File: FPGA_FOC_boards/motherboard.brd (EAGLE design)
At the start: 76.2 x 80 mm, 148 parts, among them J1 PRIUS_INV_DB26, U1 ADS7883, U10 ADS7883, U11 ADS7883, U12 ADS7883, U13 LM7321, U14 LM7321, U15 LM7321, U16 LM7321, U17 CD40109BPWR, U18 CD40109BPWR, U19 LM7321, U2 ADS7883, U20 CMOD_A7, U3 ADS7883, U4 ADS7883, U5 LM7321, U6 LM7321, U7 LM7321, U8 LM7321, U9 ADS7883

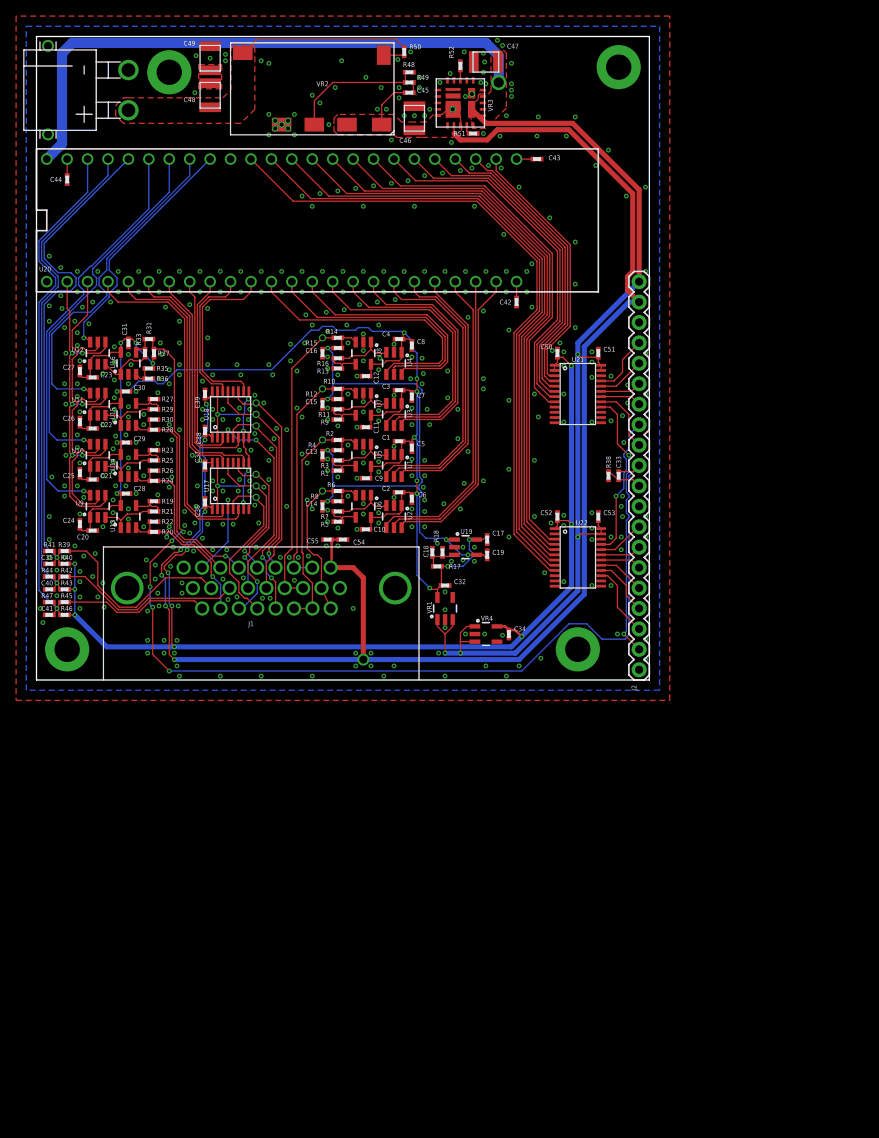
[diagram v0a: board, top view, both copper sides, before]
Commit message: started adding in the resolver hardware onto the motherboard, began ripping up some parts of the v1 board to make room for resolver hardware
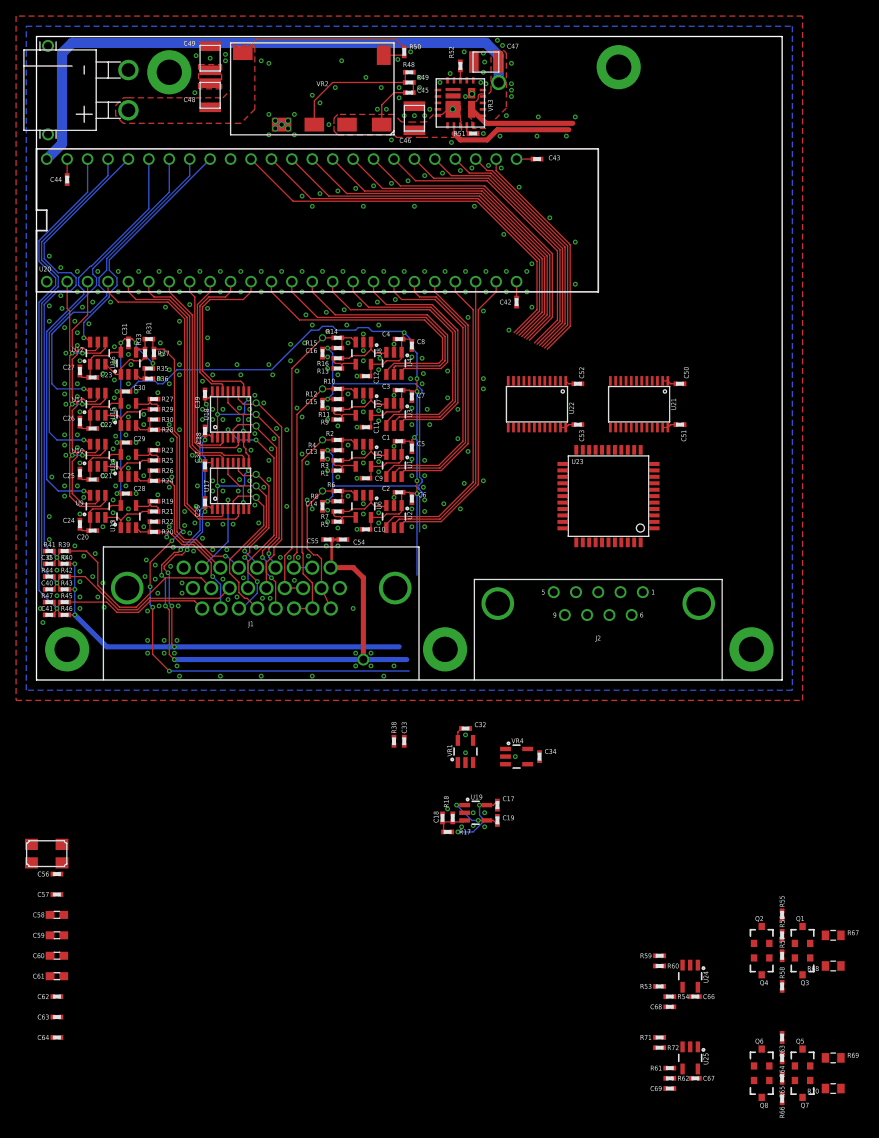
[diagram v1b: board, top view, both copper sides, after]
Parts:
- added C56, C57: 20p, FPGA_FOC_lib:0402
- added C58, C59, C60, C61: 10u, FPGA_FOC_lib:0603
- added C62, C63, C64: 10n, FPGA_FOC_lib:0402
- added C66, C67, C68, C69, R53, R54, R55, R56, R57, R58, R61, R62, R63, R64, R65, R66: (no value), FPGA_FOC_lib:0402
- added H5: BOLTHOLE_M3, FPGA_FOC_lib:M3_HOLE
- added Q1, Q2, Q3, Q4, Q5, Q6, Q7, Q8: (no value), FPGA_FOC_lib:SOT23-3
- added R59, R60, R71, R72: 1k, FPGA_FOC_lib:0402
- added R67, R68, R69, R70: 16, FPGA_FOC_lib:0805
- added U23: ADS1205, FPGA_FOC_lib:LQFP44
- added U24, U25: LM7321, FPGA_FOC_lib:SOT23-5
- added Y1: 8.192mHz, FPGA_FOC_lib:5X3.2MM_SMD_XTAL
- J2: value (none) -> DB09_RA; device FPGA_FOC_lib:1X20 -> FPGA_FOC_lib:AE10921
- R36: value (none) -> 10k
- moved C33 42.4 mm to (45.7, -7.62)
- moved R38 42.4 mm to (44.5, -7.62)
- moved U19 33.0 mm to (54.6, -16.5)
- moved C17 33.0 mm to (57.3, -15.6)
- moved C18 33.0 mm to (50.5, -17.1)
- moved C19 33.0 mm to (57.3, -17.5)
- moved R17 33.0 mm to (51.1, -18.9)
- moved R18 33.0 mm to (51.8, -17.1)
- moved U22 19.7 mm to (62.2, 34.3), turned to 270 degrees
- moved C32 18.0 mm to (53.3, -6.03)
- moved VR1 18.0 mm to (53.3, -8.89)
- moved C52 16.7 mm to (67.3, 36.8), turned to 0 degrees
- moved H1 16.5 mm to (50.8, 3.81)
- moved C50 15.7 mm to (80.0, 36.8), turned to 0 degrees
- moved C34 15.7 mm to (62.5, -9.53)
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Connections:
- new net !RD_EXC: R61.1, U23.35
- new net !RD_EXCOUT: C69.2, J2.9, R62.1, R69.2, R70.1
- new net MT1: J2.6
- new net MT2: J2.7
- new net M_CASE: J2.8
- new net Q1_BASE: Q1.1, R55.2, R56.1
- new net Q1_EMITTER: Q1.2, R67.1
- new net Q2_BC: Q2.1, Q2.3, R56.2
- new net Q3_BASE: Q3.1, R57.2, R58.1
- new net Q3_EMITTER: Q3.2, R68.2
- new net Q4_BC: Q4.1, Q4.3, R57.1
- new net Q5_BASE: Q5.1, R63.1, R64.2
- new net Q5_EMITTER: Q5.2, R69.1
- new net Q6_BC: Q6.1, Q6.3, R64.1
- new net Q7_BASE: Q7.1, R65.1, R66.2
- new net Q7_EMITTER: Q7.2, R70.2
- new net Q8_BC: Q8.1, Q8.3, R65.2
- new net RD_CLKIN: C57.1, U23.22, Y1.3
- new net RD_COS: J2.1, U23.41
- new net RD_COSLO: J2.2, U23.40
- new net RD_CPO: U23.24
- new net RD_EXC: R53.1, U23.34
- new net RD_EXCOUT: C68.2, J2.5, R54.1, R67.2, R68.1
- new net RD_REFBYP: C58.1, U23.43
- new net RD_SIN: J2.4, U23.37
- new net RD_SINLO: J2.3, U23.38
- new net RD_XTALOUT: C56.2, U23.21, Y1.1
- new net U24_IN+: R59.2, R60.1, U24.3
- new net U24_IN-: C68.1, R53.2, R54.2, U24.4
- new net U24_OUT: Q2.2, Q4.2, U24.1
- new net U25_IN+: R71.2, R72.1, U25.3
- new net U25_IN-: C69.1, R61.2, R62.2, U25.4
- new net U25_OUT: Q6.2, Q8.2, U25.1
- net !RD_CS: now also U23.3; no longer J2.16
- net !RD_DOS: now also U23.29; no longer J2.4
- net !RD_LOT: now also U23.30; no longer J2.3
- net !RD_RD: now also U23.2; no longer J2.17
- net !RD_RDVEL: now also U23.5; no longer J2.14
- net !RD_RESET: now also U23.33; no longer J2.2
- net !RD_SAMPLE: now also U23.4; no longer J2.15
- net 12V: now also C66.1, C67.1, Q1.3, Q5.3, R55.1, R63.2, U24.5, U25.5; no longer J2.19
- net 5V: now also C59.1, C60.1, C61.1, C62.1, C63.1, C64.1, R59.1, R71.1, U23.1, U23.17, U23.31, U23.32, U23.39; no longer J2.20
- net GND: now also C56.1, C57.2, C58.2, C59.2, C60.2, C61.2, C62.2, C63.2, C64.2, C66.2, C67.2, H5.P, J2.ML, J2.MR, Q3.3, Q7.3, R58.2, R60.2, R66.1, R72.2, U23.16, U23.23, U23.36, U23.42, U23.6, U24.2, U25.2, Y1.2, Y1.4; no longer J2.1, J2.18, J2.9
- net RD_A: now also U23.25; no longer J2.8
- net RD_B: now also U23.26; no longer J2.7
- net RD_DIR: now also U23.28; no longer J2.5
- net RD_MT1: no longer J2.11
- net RD_MT2: no longer J2.10
- net RD_NM: now also U23.27; no longer J2.6
- net RD_SCLK: now also U23.8; no longer J2.12
- net RD_SO: now also U23.7; no longer J2.13
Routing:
- net 5V: track 193.1 -> 89.7 mm, vias 5 -> 1
- net 12V: track 200.5 -> 109.6 mm
- net 3.3V: track 145.7 -> 86.0 mm, vias 12 -> 9
- net RD_MT1: track 132.3 -> 76.3 mm
- net !RD_RESET: track 33.8 -> 0.00 mm, vias 2 -> 0
- net !RD_LOT_LV: track 82.9 -> 50.9 mm
- net !RD_DOS_LV: track 80.0 -> 48.9 mm
- net RD_DIR_LV: track 77.1 -> 47.0 mm
- net RD_NM_LV: track 74.2 -> 45.0 mm
- net RD_B_LV: track 71.3 -> 43.0 mm
- net RD_A_LV: track 68.4 -> 41.0 mm
- net RD_SO_LV: track 65.5 -> 39.1 mm
- net RD_SO: track 17.8 -> 0.00 mm, vias 1 -> 0
- net !RD_LOT: track 9.04 -> 0.00 mm
- net !RD_RESET_LV: track 46.5 -> 37.7 mm
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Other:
- board size 76.2 x 80 mm -> 92.7 x 80 mm

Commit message: started the CCU board
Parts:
- added C65, C70, C71: 1u, FPGA_FOC_lib:0402
- added C72: 10n, FPGA_FOC_lib:0402
- added J3, J4: (no value), FPGA_FOC_lib:SM04B-SRSS-TB
- added R32: 120, FPGA_FOC_lib:0402
- added SJ1: (no value), FPGA_FOC_lib:SJ_2S-NO
- added TP11: !EXCOUT, FPGA_FOC_lib:1X01_50MIL
- added TP12: EXCOUT, FPGA_FOC_lib:1X01_50MIL
- added U26: SN65HVD23X, FPGA_FOC_lib:SOIC_8
- C66, C67: value (none) -> 1u
- C68, C69: value (none) -> DNP
- R53, R61: value (none) -> 1k
- R54, R62: value (none) -> 2.4k
- R55, R58, R63, R66: value (none) -> 2.2k
- R56, R57, R64, R65: value (none) -> 3.3
- R59, R71: value 1k -> 10k
- R60, R72: value 1k -> 4.16k
- R67: value 16 -> 4.7k
- R68, R69, R70: value 16 -> 4.7
- moved R68 34.1 mm to (65.1, -38.4)
- moved R67 31.4 mm to (68.4, -38.4), turned to 180 degrees
- moved Q3 29.8 mm to (65.4, -35.6), turned to 90 degrees
- moved R58 28.9 mm to (64.3, -33.0)
- moved R70 27.8 mm to (74.1, -38.4)
- moved R66 27.3 mm to (73.2, -33.0)
- moved C67 27.2 mm to (74.0, -23.5), turned to 90 degrees
- moved Q1 26.3 mm to (69.2, -35.6), turned to 270 degrees
- moved R57 26.2 mm to (66.5, -33.0)
- moved Q7 25.9 mm to (74.3, -35.6), turned to 90 degrees
- moved Q8 25.8 mm to (74.3, -30.5), turned to 90 degrees
- moved Q4 25.3 mm to (65.4, -30.5), turned to 90 degrees
- moved R56 24.6 mm to (68.1, -33.0), turned to 90 degrees
- moved C69 24.1 mm to (77.9, -26.7)
- moved R65 23.9 mm to (75.4, -33.0)
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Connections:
- new net CANH: J3.2, J4.2, R32.1, U26.7
- new net CANL: J3.1, J4.1, SJ1.2, U26.6
- new net CAN_RS: U26.8
- new net CAN_RXD: U26.4
- new net CAN_TXD: U26.1
- new net CAN_VREF: U26.5
- new net N$2: R32.2, SJ1.1
- net !RD_EXCOUT: now also TP11.1
- net 12V: now also C65.1, C70.1, R59.1, R71.1
- net 3.3V: now also C71.1, C72.1, U26.3
- net 5V: now also J3.4, J4.4; no longer R59.1, R71.1
- net GND: now also C65.2, C70.2, C71.2, C72.2, J3.3, J4.3, U26.2
- net RD_EXCOUT: now also TP12.1
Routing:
- net !RD_RD_LV: track 28.7 -> 14.5 mm
- net !RD_CS_LV: track 29.8 -> 15.9 mm
- net !RD_SAMPLE_LV: track 31.8 -> 18.2 mm
- net !RD_RDVEL_LV: track 33.7 -> 20.5 mm
- net RD_SCLK_LV: track 35.7 -> 22.8 mm
- net !RD_RESET_LV: track 37.7 -> 25.1 mm
- net RD_SO_LV: track 39.1 -> 27.1 mm
- net RD_A_LV: track 41.0 -> 29.4 mm
- net RD_B_LV: track 43.0 -> 31.7 mm
- net RD_NM_LV: track 45.0 -> 34.0 mm
- net RD_DIR_LV: track 47.0 -> 36.2 mm
- net !RD_DOS_LV: track 48.9 -> 38.5 mm
- net !RD_LOT_LV: track 50.9 -> 40.8 mm
